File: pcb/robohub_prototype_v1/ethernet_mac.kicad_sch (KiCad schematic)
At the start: 43 parts, among them U41 KSZ8081RNB, U42 SI-60110-F, X41 ECS-2520MV-xxx-xx

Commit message: Update paths to footprint libraries. Begin adding footprints for PDN resistors. Create master BOM
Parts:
- U41: footprint custom_footprint:KSZ8081RNB -> fryelabs:KSZ8081RNB
- U42: footprint custom_footprint:SI-60110-F -> fryelabs:SI-60110-F
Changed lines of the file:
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@@
 			)
 		)
-		(property "Footprint" "custom_footprint:KSZ8081RNB"
+		(property "Footprint" "fryelabs:KSZ8081RNB"
 			(at 83.82 93.98 0)
 			(effects
@@
 			)
 		)
-		(property "Footprint" "custom_footprint:SI-60110-F"
+		(property "Footprint" "fryelabs:SI-60110-F"
 			(at 72.39 170.18 0)
 			(effects

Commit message: Begin PDN circuit design/BOM/layout
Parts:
- U41: footprint fryelabs:KSZ8081RNB -> fryelabs_kicad_footprint_lib:KSZ8081RNB
- U42: footprint fryelabs:SI-60110-F -> fryelabs_kicad_footprint_lib:SI-60110-F
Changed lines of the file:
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@@
 			)
 		)
-		(property "Footprint" "fryelabs:KSZ8081RNB"
+		(property "Footprint" "fryelabs_kicad_footprint_lib:KSZ8081RNB"
 			(at 83.82 93.98 0)
 			(effects
@@
 			)
 		)
-		(property "Footprint" "fryelabs:SI-60110-F"
+		(property "Footprint" "fryelabs_kicad_footprint_lib:SI-60110-F"
 			(at 72.39 170.18 0)
 			(effects

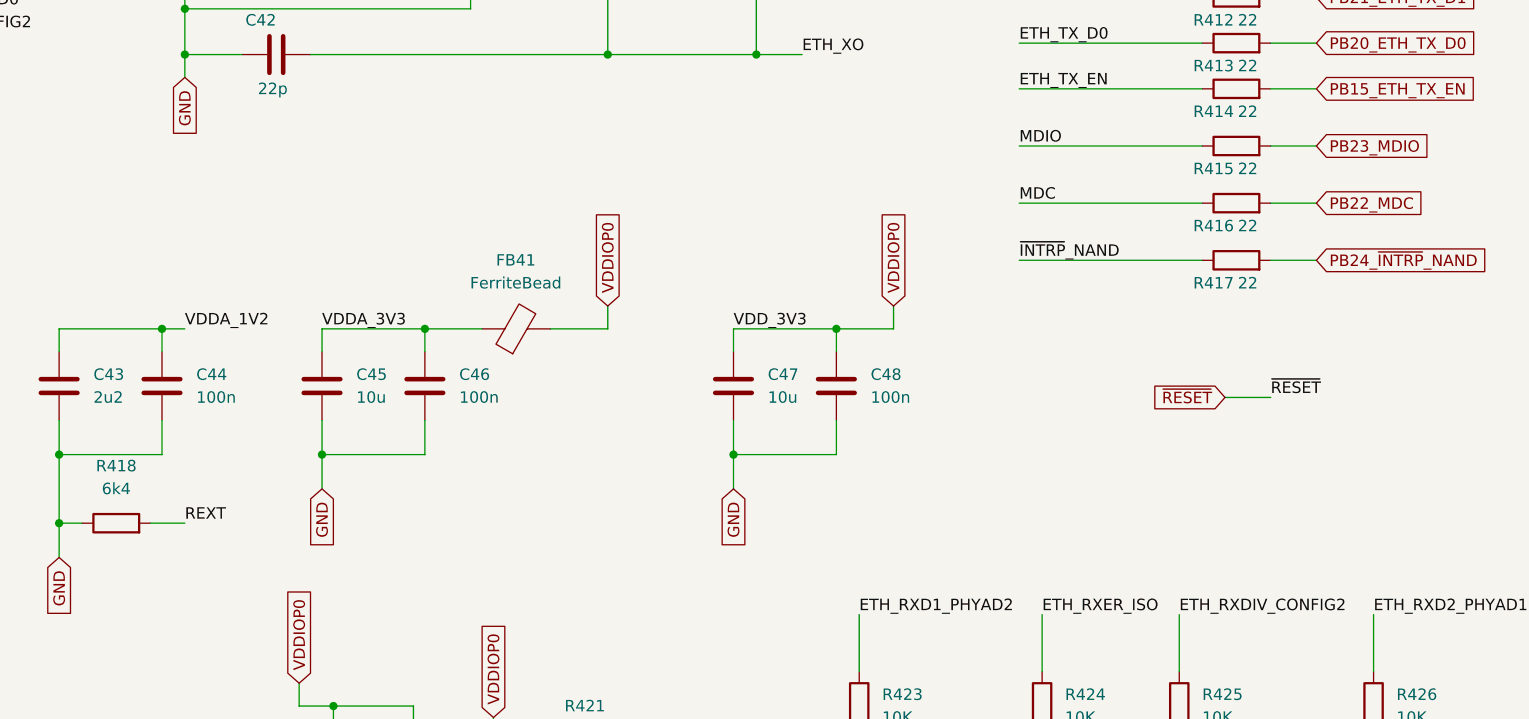
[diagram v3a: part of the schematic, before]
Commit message: Start routing ddr2
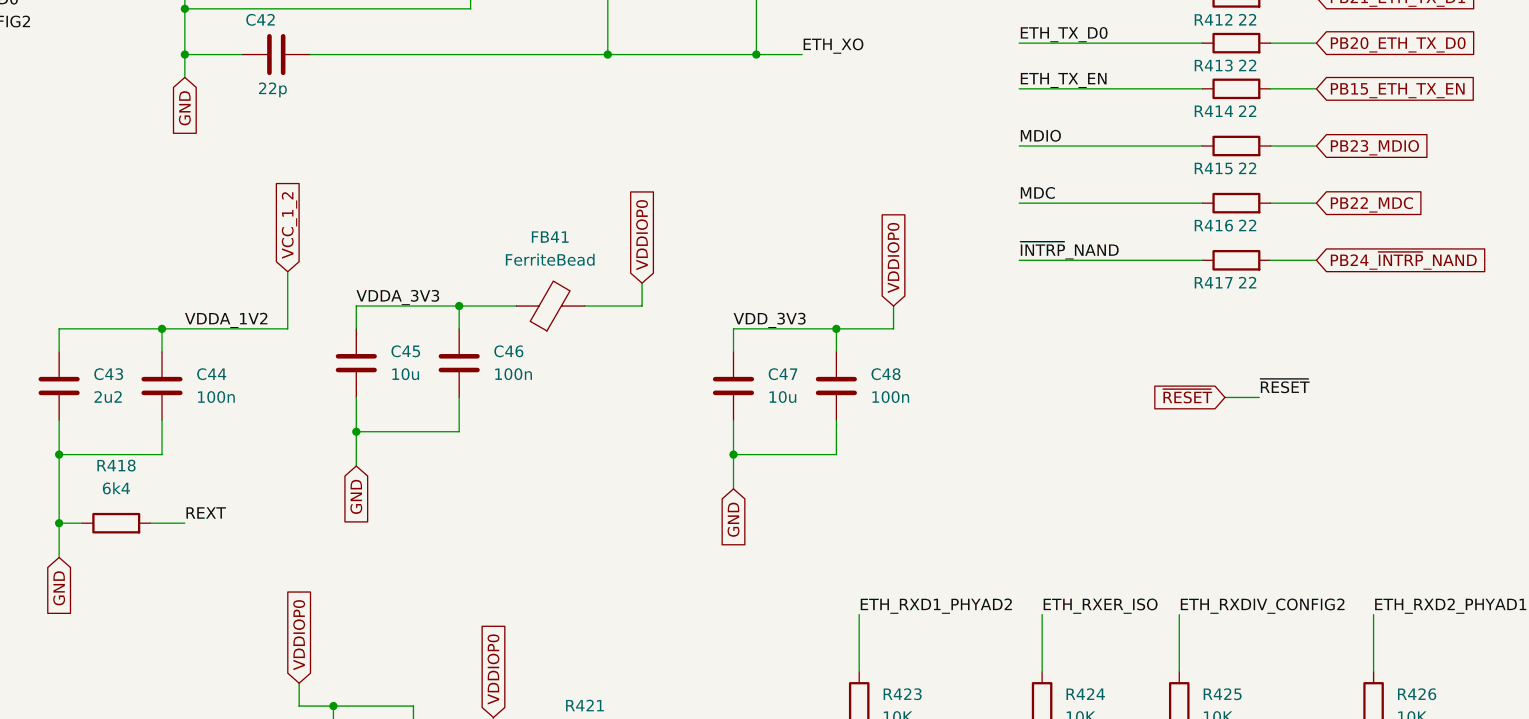
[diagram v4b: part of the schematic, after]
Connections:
- net VDDA_1V2 renamed VCC_1_2
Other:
- moved on the sheet: C45, C46, FB41
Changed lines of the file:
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@@
 	)
 	(junction
-		(at 137.16 107.95)
+		(at 140.97 105.41)
 		(diameter 0)
 		(color 0 0 0 0)
 	)
 	(junction
-		(at 125.73 121.92)
+		(at 129.54 119.38)
 		(diameter 0)
 		(color 0 0 0 0)
@@
 	(wire
 		(pts
-			(xy 157.48 105.41) (xy 157.48 107.95)
+			(xy 161.29 102.87) (xy 161.29 105.41)
 		)
 		(stroke
@@
 	(wire
 		(pts
-			(xy 125.73 107.95) (xy 137.16 107.95)
+			(xy 129.54 105.41) (xy 140.97 105.41)
 		)
 		(stroke
@@
 	(wire
 		(pts
-			(xy 125.73 110.49) (xy 125.73 107.95)
+			(xy 129.54 107.95) (xy 129.54 105.41)
 		)
 		(stroke
@@
 	(wire
 		(pts
-			(xy 125.73 121.92) (xy 125.73 118.11)
+			(xy 129.54 119.38) (xy 129.54 115.57)
 		)
 		(stroke
@@
 	(wire
 		(pts
-			(xy 151.13 107.95) (xy 157.48 107.95)
+			(xy 154.94 105.41) (xy 161.29 105.41)
 		)
 		(stroke
@@
 	(wire
 		(pts
-			(xy 137.16 107.95) (xy 137.16 110.49)
+			(xy 140.97 105.41) (xy 140.97 107.95)
 		)
 		(stroke
@@
 	(wire
 		(pts
-			(xy 226.06 115.57) (xy 231.14 115.57)
+			(xy 226.06 115.57) (xy 229.87 115.57)
 		)
 		(stroke
@@
 	(wire
 		(pts
-			(xy 137.16 118.11) (xy 137.16 121.92)
+			(xy 140.97 115.57) (xy 140.97 119.38)
 		)
 		(stroke
@@
 	(wire
 		(pts
+			(xy 121.92 101.6) (xy 121.92 107.95)
+		)
+		(stroke
+			(width 0)
+			(type default)
+		)
+	)
+	(wire
+		(pts
 			(xy 99.06 180.34) (xy 91.44 180.34)
 		)
@@
 	(wire
 		(pts
-			(xy 137.16 121.92) (xy 125.73 121.92)
+			(xy 140.97 119.38) (xy 129.54 119.38)
 		)
 		(stroke
@@
 	(wire
 		(pts
-			(xy 125.73 121.92) (xy 125.73 125.73)
+			(xy 129.54 119.38) (xy 129.54 123.19)
 		)
 		(stroke
@@
 	(wire
 		(pts
-			(xy 137.16 107.95) (xy 143.51 107.95)
+			(xy 140.97 105.41) (xy 147.32 105.41)
 		)
 		(stroke
@@
 	(wire
 		(pts
-			(xy 107.95 107.95) (xy 110.49 107.95)
+			(xy 107.95 107.95) (xy 121.92 107.95)
 		)
 		(stroke
@@
 	)
 	(label "~{RESET}"
-		(at 231.14 115.57 0)
+		(at 229.87 115.57 0)
 		(fields_autoplaced yes)
 		(effects
@@
 	)
 	(label "VDDA_3V3"
-		(at 125.73 107.95 0)
+		(at 129.54 105.41 0)
 		(fields_autoplaced yes)
 		(effects
@@
 	(global_label "VDDIOP0"
 		(shape input)
-		(at 157.48 105.41 90)
+		(at 161.29 102.87 90)
 		(fields_autoplaced yes)
 		(effects
@@
 		)
 		(property "Intersheetrefs" "${INTERSHEET_REFS}"
-			(at 157.4006 94.9536 90)
+			(at 161.2106 92.4136 90)
 			(effects
 				(font
@@
 		)
 	)
+	(global_label "VCC_1_2"
+		(shape input)
+		(at 121.92 101.6 90)
+		(fields_autoplaced yes)
+		(effects
+			(font
+				(size 1.27 1.27)
+			)
+			(justify left)
+		)
+		(property "Intersheetrefs" "${INTERSHEET_REFS}"
+			(at 121.8406 91.204 90)
+			(effects
+				(font
+					(size 1.27 1.27)
+				)
+				(justify left)
+				(hide yes)
+			)
+		)
+	)
 	(global_label "VDDIOP0"
 		(shape input)
@@
 	(global_label "GND"
 		(shape input)
-		(at 125.73 125.73 270)
+		(at 129.54 123.19 270)
 		(fields_autoplaced yes)
 		(effects
@@
 		)
 		(property "Intersheetrefs" "${INTERSHEET_REFS}"
-			(at 125.6506 132.0136 90)
+			(at 129.4606 129.4736 90)
 			(effects
 				(font
@@
 	(symbol
 		(lib_id "Device:C")
-		(at 137.16 114.3 0)
+		(at 140.97 111.76 0)
 		(unit 1)
 		(exclude_from_sim no)
@@
 		(fields_autoplaced yes)
 		(property "Reference" "C46"
-			(at 140.97 113.03 0)
+			(at 144.78 110.49 0)
 			(effects
 				(font
@@
 		)
 		(property "Value" "100n"
-			(at 140.97 115.57 0)
+			(at 144.78 113.03 0)
 			(effects
 				(font
@@
 		)
 		(property "Footprint" ""
-			(at 138.1252 118.11 0)
+			(at 141.9352 115.57 0)
 			(effects
 				(font
@@
 		)
 		(property "Datasheet" "~"
-			(at 137.16 114.3 0)
+			(at 140.97 111.76 0)
 			(effects
 				(font
@@
 		)
 		(property "Description" ""
-			(at 137.16 114.3 0)
+			(at 140.97 111.76 0)
 			(effects
 				(font
@@
 	(symbol
 		(lib_id "Device:FerriteBead")
-		(at 147.32 107.95 90)
+		(at 151.13 105.41 90)
 		(unit 1)
 		(exclude_from_sim no)
@@
 		(dnp no)
 		(property "Reference" "FB41"
-			(at 147.2692 100.33 90)
+			(at 151.0792 97.79 90)
 			(effects
 				(font
@@
 		)
 		(property "Value" "FerriteBead"
-			(at 147.2692 102.87 90)
+			(at 151.0792 100.33 90)
 			(effects
 				(font
@@
 		)
 		(property "Footprint" ""
-			(at 147.32 109.728 90)
+			(at 151.13 107.188 90)
 			(effects
 				(font
@@
 		)
 		(property "Datasheet" "~"
-			(at 147.32 107.95 0)
+			(at 151.13 105.41 0)
 			(effects
 				(font
@@
 		)
 		(property "Description" ""
-			(at 147.32 107.95 0)
+			(at 151.13 105.41 0)
 			(effects
 				(font
@@
 	(symbol
 		(lib_id "Device:C")
-		(at 125.73 114.3 0)
+		(at 129.54 111.76 0)
 		(unit 1)
 		(exclude_from_sim no)
@@
 		(fields_autoplaced yes)
 		(property "Reference" "C45"
-			(at 129.54 113.03 0)
+			(at 133.35 110.49 0)
 			(effects
 				(font
@@
 		)
 		(property "Value" "10u"
-			(at 129.54 115.57 0)
+			(at 133.35 113.03 0)
 			(effects
 				(font
@@
 		)
 		(property "Footprint" ""
-			(at 126.6952 118.11 0)
+			(at 130.5052 115.57 0)
 			(effects
 				(font
@@
 		)
 		(property "Datasheet" "~"
-			(at 125.73 114.3 0)
+			(at 129.54 111.76 0)
 			(effects
 				(font
@@
 		)
 		(property "Description" ""
-			(at 125.73 114.3 0)
+			(at 129.54 111.76 0)
 			(effects
 				(font

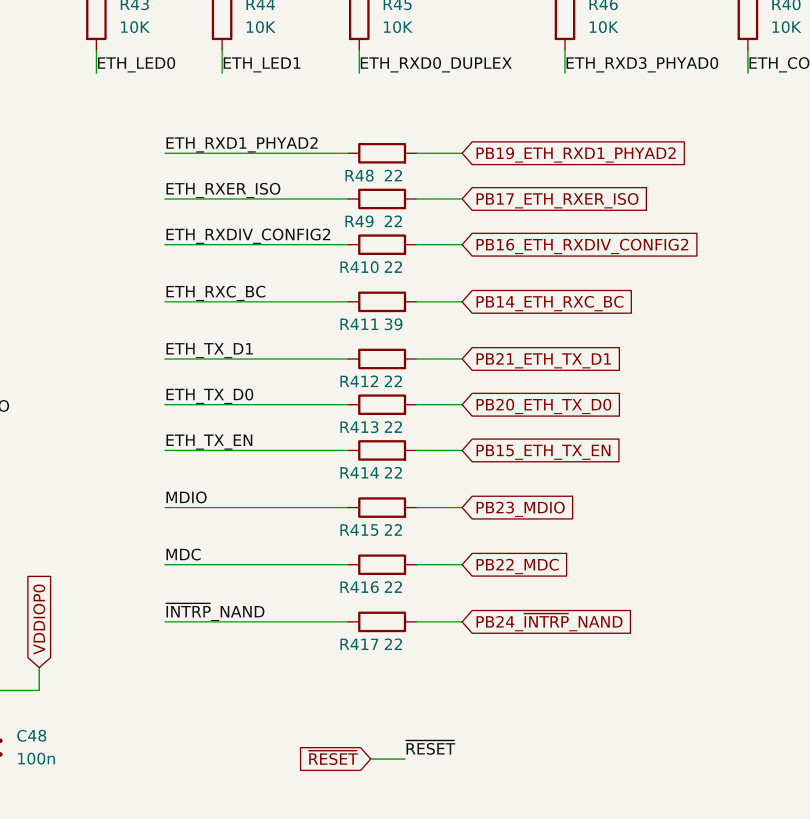
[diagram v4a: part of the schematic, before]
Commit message: Update footprint assignment. begin laying out ethernet
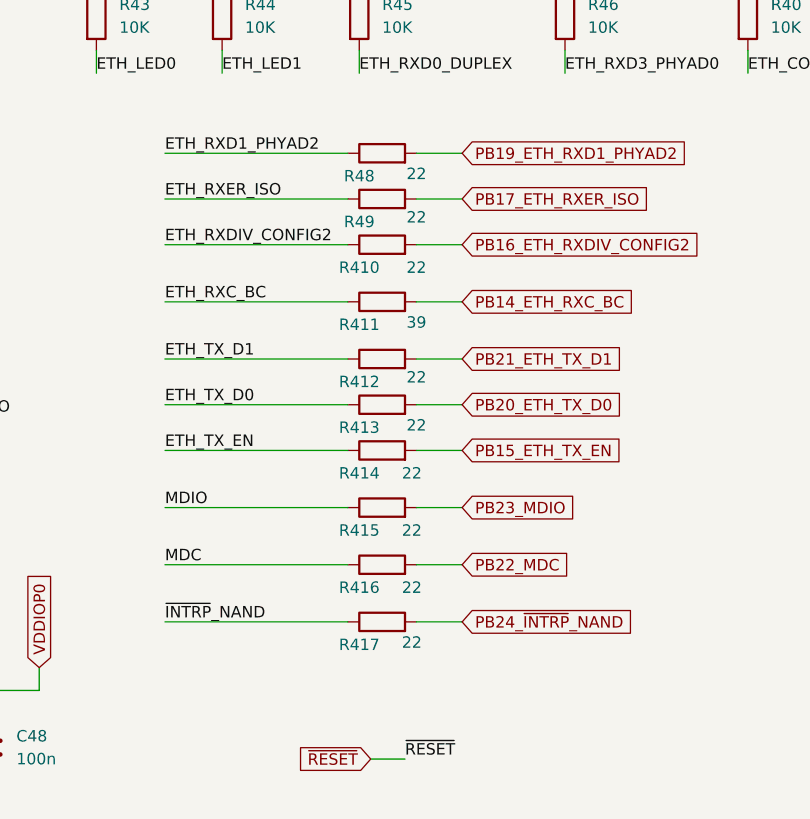
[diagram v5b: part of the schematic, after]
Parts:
- C41, C410, C42, C43, C44, C45, C46, C47, C48, C49: footprint (none) -> Capacitor_SMD:C_0402_1005Metric
- FB41, FB42: footprint (none) -> Diode_SMD:D_0402_1005Metric
- R40, R41, R410, R411, R412, R413, R414, R415, R416, R417, R418, R419, R42, R420, R421, R422, R423, R424, R425, R426, R427, R43, R44, R45, R46, R47, R48, R49: footprint (none) -> Resistor_SMD:R_0402_1005Metric
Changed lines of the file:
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@@
 			)
 		)
-		(property "Footprint" ""
+		(property "Footprint" "Resistor_SMD:R_0402_1005Metric"
 			(at 177.292 33.02 90)
 			(effects
@@
 			)
 		)
-		(property "Footprint" ""
+		(property "Footprint" "Resistor_SMD:R_0402_1005Metric"
 			(at 154.94 168.148 90)
 			(effects
@@
 			)
 		)
-		(property "Footprint" ""
+		(property "Footprint" "Capacitor_SMD:C_0402_1005Metric"
 			(at 139.3952 184.15 0)
 			(effects
@@
 			)
 		)
-		(property "Footprint" ""
+		(property "Footprint" "Resistor_SMD:R_0402_1005Metric"
 			(at 219.202 149.86 90)
 			(effects
@@
 			)
 		)
-		(property "Footprint" ""
+		(property "Footprint" "Capacitor_SMD:C_0402_1005Metric"
 			(at 108.9152 118.11 0)
 			(effects
@@
 		)
 		(property "Value" "22"
-			(at 228.6 55.88 90)
-			(effects
-				(font
-					(size 1.27 1.27)
-				)
-			)
-		)
-		(property "Footprint" ""
+			(at 231.14 55.372 90)
+			(effects
+				(font
+					(size 1.27 1.27)
+				)
+			)
+		)
+		(property "Footprint" "Resistor_SMD:R_0402_1005Metric"
 			(at 227.33 55.118 90)
 			(effects
@@
 			)
 		)
-		(property "Footprint" ""
+		(property "Footprint" "Capacitor_SMD:C_0402_1005Metric"
 			(at 126.6952 184.15 0)
 			(effects
@@
 		)
 		(property "Value" "22"
-			(at 228.6 60.96 90)
-			(effects
-				(font
-					(size 1.27 1.27)
-				)
-			)
-		)
-		(property "Footprint" ""
+			(at 231.14 60.96 90)
+			(effects
+				(font
+					(size 1.27 1.27)
+				)
+			)
+		)
+		(property "Footprint" "Resistor_SMD:R_0402_1005Metric"
 			(at 227.33 60.198 90)
 			(effects
@@
 			)
 		)
-		(property "Footprint" ""
+		(property "Footprint" "Resistor_SMD:R_0402_1005Metric"
 			(at 154.94 157.988 90)
 			(effects
@@
 		)
 		(property "Value" "22"
-			(at 228.6 102.87 90)
-			(effects
-				(font
-					(size 1.27 1.27)
-				)
-			)
-		)
-		(property "Footprint" ""
+			(at 230.632 102.616 90)
+			(effects
+				(font
+					(size 1.27 1.27)
+				)
+			)
+		)
+		(property "Footprint" "Resistor_SMD:R_0402_1005Metric"
 			(at 227.33 102.108 90)
 			(effects
@@
 			)
 		)
-		(property "Footprint" ""
+		(property "Footprint" "Resistor_SMD:R_0402_1005Metric"
 			(at 207.772 33.02 90)
 			(effects
@@
 			)
 		)
-		(property "Footprint" ""
+		(property "Footprint" "Capacitor_SMD:C_0402_1005Metric"
 			(at 141.9352 115.57 0)
 			(effects
@@
 		)
 		(property "Value" "22"
-			(at 228.6 78.74 90)
-			(effects
-				(font
-					(size 1.27 1.27)
-				)
-			)
-		)
-		(property "Footprint" ""
+			(at 231.14 78.486 90)
+			(effects
+				(font
+					(size 1.27 1.27)
+				)
+			)
+		)
+		(property "Footprint" "Resistor_SMD:R_0402_1005Metric"
 			(at 227.33 77.978 90)
 			(effects
@@
 			)
 		)
-		(property "Footprint" ""
+		(property "Footprint" "Resistor_SMD:R_0402_1005Metric"
 			(at 193.802 33.02 90)
 			(effects
@@
 			)
 		)
-		(property "Footprint" ""
+		(property "Footprint" "Capacitor_SMD:C_0402_1005Metric"
 			(at 124.46 46.0248 0)
 			(effects
@@
 			)
 		)
-		(property "Footprint" ""
+		(property "Footprint" "Resistor_SMD:R_0402_1005Metric"
 			(at 245.872 33.02 90)
 			(effects
@@
 			)
 		)
-		(property "Footprint" ""
+		(property "Footprint" "Resistor_SMD:R_0402_1005Metric"
 			(at 266.192 33.02 90)
 			(effects
@@
 		)
 		(property "Value" "22"
-			(at 228.6 83.82 90)
-			(effects
-				(font
-					(size 1.27 1.27)
-				)
-			)
-		)
-		(property "Footprint" ""
+			(at 230.632 83.82 90)
+			(effects
+				(font
+					(size 1.27 1.27)
+				)
+			)
+		)
+		(property "Footprint" "Resistor_SMD:R_0402_1005Metric"
 			(at 227.33 83.058 90)
 			(effects
@@
 			)
 		)
-		(property "Footprint" ""
+		(property "Footprint" "Resistor_SMD:R_0402_1005Metric"
 			(at 183.642 149.86 90)
 			(effects
@@
 			)
 		)
-		(property "Footprint" ""
+		(property "Footprint" "Diode_SMD:D_0402_1005Metric"
 			(at 151.13 107.188 90)
 			(effects
@@
 			)
 		)
-		(property "Footprint" ""
+		(property "Footprint" "Resistor_SMD:R_0402_1005Metric"
 			(at 172.212 62.23 90)
 			(effects
@@
 		)
 		(property "Value" "22"
-			(at 228.6 96.52 90)
-			(effects
-				(font
-					(size 1.27 1.27)
-				)
-			)
-		)
-		(property "Footprint" ""
+			(at 230.632 96.52 90)
+			(effects
+				(font
+					(size 1.27 1.27)
+				)
+			)
+		)
+		(property "Footprint" "Resistor_SMD:R_0402_1005Metric"
 			(at 227.33 95.758 90)
 			(effects
@@
 			)
 		)
-		(property "Footprint" ""
+		(property "Footprint" "Capacitor_SMD:C_0402_1005Metric"
 			(at 130.5052 115.57 0)
 			(effects
@@
 		)
 		(property "Value" "22"
-			(at 228.6 50.8 90)
-			(effects
-				(font
-					(size 1.27 1.27)
-				)
-			)
-		)
-		(property "Footprint" ""
+			(at 231.14 50.546 90)
+			(effects
+				(font
+					(size 1.27 1.27)
+				)
+			)
+		)
+		(property "Footprint" "Resistor_SMD:R_0402_1005Metric"
 			(at 227.33 50.038 90)
 			(effects
@@
 			)
 		)
-		(property "Footprint" ""
+		(property "Footprint" "Capacitor_SMD:C_0402_1005Metric"
 			(at 124.46 76.5048 0)
 			(effects
@@
 			)
 		)
-		(property "Footprint" ""
+		(property "Footprint" "Resistor_SMD:R_0402_1005Metric"
 			(at 262.382 149.86 90)
 			(effects
@@
 			)
 		)
-		(property "Footprint" ""
+		(property "Footprint" "Capacitor_SMD:C_0402_1005Metric"
 			(at 172.4152 118.11 0)
 			(effects
@@
 			)
 		)
-		(property "Footprint" ""
+		(property "Footprint" "Resistor_SMD:R_0402_1005Metric"
 			(at 240.792 149.86 90)
 			(effects
@@
 		)
 		(property "Value" "39"
-			(at 228.6 67.31 90)
-			(effects
-				(font
-					(size 1.27 1.27)
-				)
-			)
-		)
-		(property "Footprint" ""
+			(at 231.14 67.056 90)
+			(effects
+				(font
+					(size 1.27 1.27)
+				)
+			)
+		)
+		(property "Footprint" "Resistor_SMD:R_0402_1005Metric"
 			(at 227.33 66.548 90)
 			(effects
@@
 			)
 		)
-		(property "Footprint" ""
+		(property "Footprint" "Resistor_SMD:R_0402_1005Metric"
 			(at 223.012 33.02 90)
 			(effects
@@
 			)
 		)
-		(property "Footprint" ""
+		(property "Footprint" "Resistor_SMD:R_0402_1005Metric"
 			(at 102.87 131.318 90)
 			(effects
@@
 		)
 		(property "Value" "22"
-			(at 228.6 90.17 90)
-			(effects
-				(font
-					(size 1.27 1.27)
-				)
-			)
-		)
-		(property "Footprint" ""
+			(at 230.632 90.17 90)
+			(effects
+				(font
+					(size 1.27 1.27)
+				)
+			)
+		)
+		(property "Footprint" "Resistor_SMD:R_0402_1005Metric"
 			(at 227.33 89.408 90)
 			(effects
@@
 			)
 		)
-		(property "Footprint" ""
+		(property "Footprint" "Resistor_SMD:R_0402_1005Metric"
 			(at 125.222 158.75 90)
 			(effects
@@
 			)
 		)
-		(property "Footprint" ""
+		(property "Footprint" "Resistor_SMD:R_0402_1005Metric"
 			(at 134.112 158.75 90)
 			(effects
@@
 		)
 		(property "Value" "22"
-			(at 228.6 73.66 90)
-			(effects
-				(font
-					(size 1.27 1.27)
-				)
-			)
-		)
-		(property "Footprint" ""
+			(at 231.14 73.152 90)
+			(effects
+				(font
+					(size 1.27 1.27)
+				)
+			)
+		)
+		(property "Footprint" "Resistor_SMD:R_0402_1005Metric"
 			(at 227.33 72.898 90)
 			(effects
@@
 			)
 		)
-		(property "Footprint" ""
+		(property "Footprint" "Capacitor_SMD:C_0402_1005Metric"
 			(at 97.4852 118.11 0)
 			(effects
@@
 			)
 		)
-		(property "Footprint" ""
+		(property "Footprint" "Resistor_SMD:R_0402_1005Metric"
 			(at 162.052 33.02 90)
 			(effects
@@
 			)
 		)
-		(property "Footprint" ""
+		(property "Footprint" "Capacitor_SMD:C_0402_1005Metric"
 			(at 183.8452 118.11 0)
 			(effects
@@
 			)
 		)
-		(property "Footprint" ""
+		(property "Footprint" "Resistor_SMD:R_0402_1005Metric"
 			(at 203.962 149.86 90)
 			(effects
@@
 			)
 		)
-		(property "Footprint" ""
+		(property "Footprint" "Diode_SMD:D_0402_1005Metric"
 			(at 102.87 182.118 90)
 			(effects
